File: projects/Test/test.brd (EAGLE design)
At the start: 63.5 x 24.1 mm, 47 parts, among them J2 1755529, U1 STM32F405RGT6, U2 CSD88584Q5DCT, U3 CSD88584Q5DCT, U4 CSD88584Q5DCT, Y1 ECS-80-S-4X

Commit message: some stuff
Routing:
- net 3V3: track 76.5 -> 71.3 mm, vias 8 -> 7
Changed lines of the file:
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@@
 <via x="34.29" y="16.764" extent="1-16" drill="0.35"/>
 <via x="46.482" y="16.256" extent="1-16" drill="0.35"/>
-<via x="46.482" y="5.461" extent="1-16" drill="0.35"/>
+<via x="46.482" y="5.969" extent="1-16" drill="0.35"/>
 <via x="34.417" y="6.223" extent="1-16" drill="0.35"/>
 </signal>
@@
 <wire x1="44.136" y1="15.053" x2="43.815" y2="14.732" width="0.2032" layer="1"/>
 <via x="43.815" y="14.732" extent="1-16" drill="0.35"/>
-<via x="37.6682" y="15.2301" extent="1-16" drill="0.35"/>
-<wire x1="38.136" y1="16.5481" x2="38.136" y2="15.6979" width="0.2032" layer="1"/>
-<wire x1="38.136" y1="15.6979" x2="37.6682" y2="15.2301" width="0.2032" layer="1"/>
-<wire x1="43.815" y1="14.732" x2="43.307" y2="14.224" width="0.2032" layer="16"/>
-<wire x1="43.307" y1="14.224" x2="42.4044" y2="14.224" width="0.2032" layer="16"/>
+<wire x1="38.136" y1="15.6979" x2="38.136" y2="16.5481" width="0.2032" layer="1"/>
 <wire x1="37.25" y1="14.224" x2="37.25" y2="14.6341" width="0.2032" layer="16"/>
-<wire x1="37.25" y1="14.6341" x2="37.8714" y2="15.2555" width="0.2032" layer="16"/>
-<via x="37.8714" y="15.2555" extent="1-16" drill="0.35"/>
-<wire x1="38.136" y1="16.5481" x2="38.136" y2="15.5201" width="0.2032" layer="1"/>
-<wire x1="38.136" y1="15.5201" x2="37.8714" y2="15.2555" width="0.2032" layer="1"/>
-<wire x1="37.25" y1="14.224" x2="36.576" y2="14.224" width="0.2032" layer="16"/>
-<wire x1="36.576" y1="14.224" x2="36.068" y2="13.716" width="0.2032" layer="16"/>
 <via x="36.068" y="13.716" extent="1-16" drill="0.35"/>
 <wire x1="34.7599" y1="13.672" x2="36.024" y2="13.672" width="0.2032" layer="1"/>
@@
 <wire x1="40.64" y1="12.4578" x2="42.3418" y2="12.4578" width="0.4064" layer="16"/>
 <wire x1="42.3418" y1="12.4578" x2="42.3858" y2="12.4138" width="0.4064" layer="16"/>
-<wire x1="37.6682" y1="15.2301" x2="37.25" y2="14.8119" width="0.2032" layer="16"/>
-<wire x1="37.25" y1="14.8119" x2="37.25" y2="14.224" width="0.2032" layer="16"/>
+<wire x1="37.25" y1="14.224" x2="37.25" y2="14.8119" width="0.2032" layer="16"/>
 <wire x1="36.068" y1="13.716" x2="36.576" y2="14.224" width="0.2032" layer="16"/>
 <wire x1="36.576" y1="14.224" x2="37.25" y2="14.224" width="0.2032" layer="16"/>
@@
 <wire x1="43.815" y1="14.732" x2="43.307" y2="14.224" width="0.2032" layer="16"/>
 <wire x1="43.307" y1="14.224" x2="42.4044" y2="14.224" width="0.2032" layer="16"/>
+<wire x1="37.25" y1="14.8119" x2="37.6781" y2="15.24" width="0.2032" layer="16"/>
+<wire x1="37.6781" y1="15.24" x2="37.719" y2="15.24" width="0.2032" layer="16"/>
+<via x="37.719" y="15.24" extent="1-16" drill="0.35"/>
+<wire x1="37.719" y1="15.24" x2="37.719" y2="15.2809" width="0.2032" layer="1"/>
+<wire x1="37.719" y1="15.2809" x2="38.136" y2="15.6979" width="0.2032" layer="1"/>
 </signal>
 <signal name="N$5">
@@
 <contactref element="U$2" pad="28"/>
 <wire x1="31.5468" y1="6.5532" x2="33.274" y2="4.826" width="0.2032" layer="1"/>
-<wire x1="33.274" y1="4.826" x2="36.1661" y2="4.826" width="0.2032" layer="1"/>
-<wire x1="36.1661" y1="4.826" x2="36.636" y2="5.2959" width="0.2032" layer="1"/>
+<wire x1="33.274" y1="4.826" x2="36.5471" y2="4.826" width="0.2032" layer="1"/>
+<wire x1="36.636" y1="4.9149" x2="36.636" y2="5.2959" width="0.2032" layer="1"/>
+<wire x1="36.636" y1="4.9149" x2="36.5471" y2="4.826" width="0.2032" layer="1"/>
 <wire x1="28.662" y1="8.148" x2="28.7149" y2="8.0951" width="0.2032" layer="1"/>
 <wire x1="28.7149" y1="8.0951" x2="29.18825" y2="8.0951" width="0.2032" layer="1"/>
@@
 <mfgpreviewcolor name="substratecolor" color="0xFF786E46"/>
 </mfgpreviewcolors>
-<errors>
-</errors>
 </board>
 </drawing>

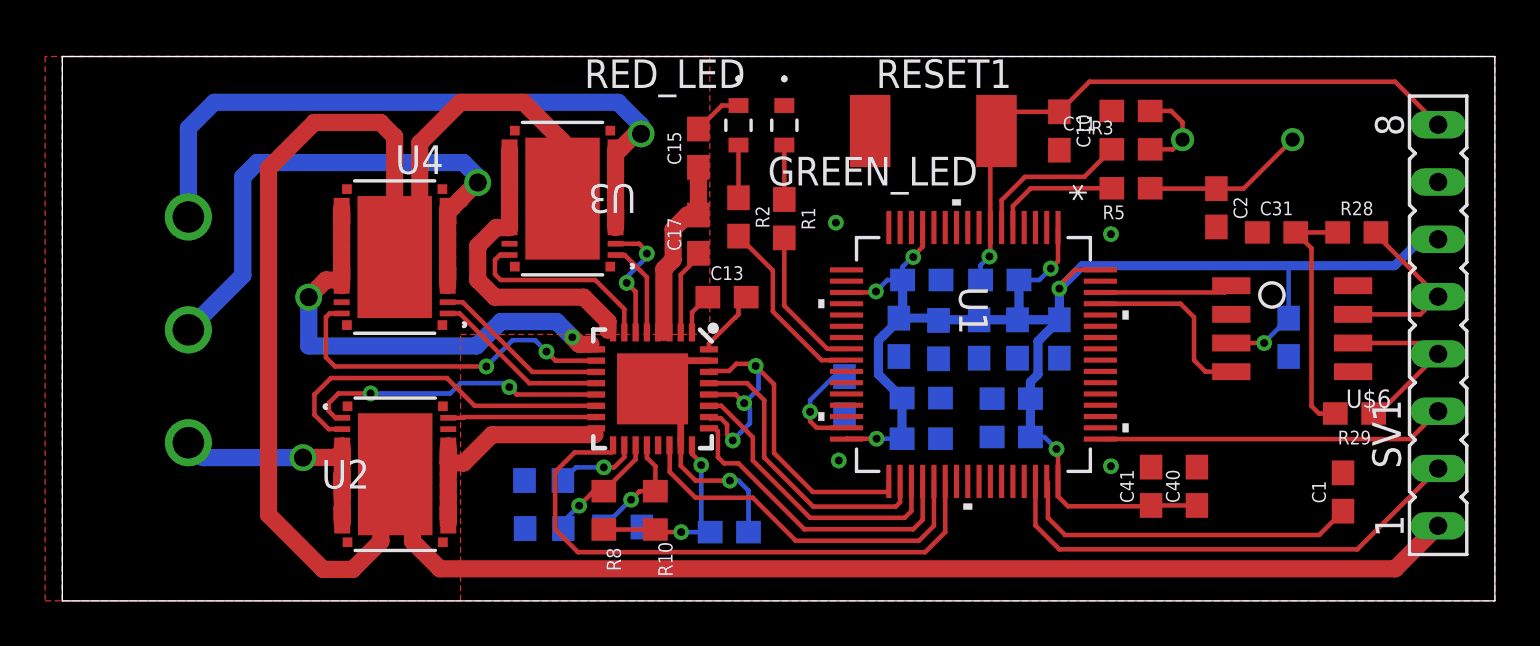
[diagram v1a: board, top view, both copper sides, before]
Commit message: Finished test board (before ratsnest)
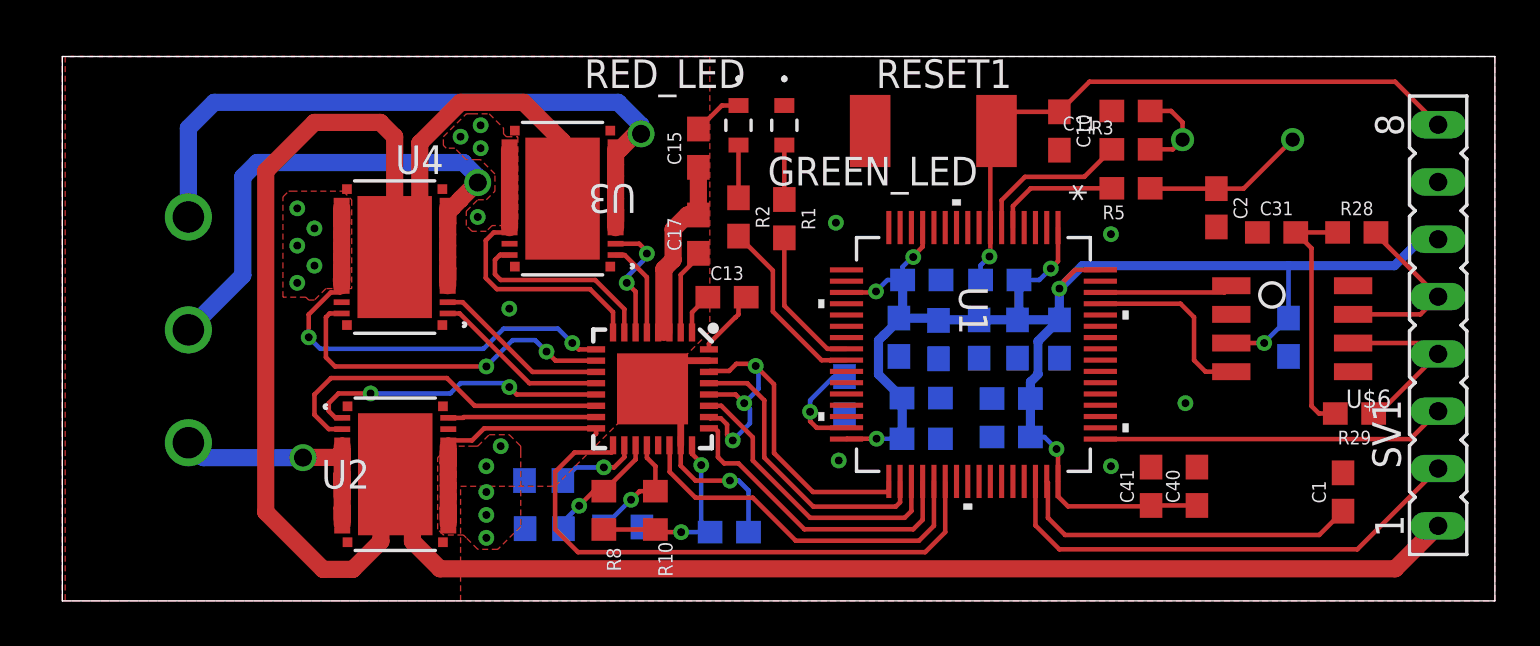
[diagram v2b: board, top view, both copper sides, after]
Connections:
- removed net SLA_1: U$2.8, U3.12, U3.13, U3.14, U3.15, U3.16, U3.17, U3.18, U3.19, U3.20
- removed net SLB_1: U$2.9, U4.12, U4.13, U4.14, U4.15, U4.16, U4.17, U4.18, U4.19, U4.20
- removed net SLC_1: U$2.16, U2.12, U2.13, U2.14, U2.15, U2.16, U2.17, U2.18, U2.19, U2.20
- net GND: now also U$2.16, U$2.8, U$2.9, U2.12, U2.13, U2.14, U2.15, U2.16, U2.17, U2.18, U2.19, U2.20, U3.12, U3.13, U3.14, U3.15, U3.16, U3.17, U3.18, U3.19, U3.20, U4.12, U4.13, U4.14, U4.15, U4.16, U4.17, U4.18, U4.19, U4.20
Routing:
- net GND: track 18.3 -> 67.7 mm, vias 5 -> 23
- net SLB_1: track 23.1 -> 0.00 mm, vias 2 -> 0
- net SLA_1: track 15.2 -> 0.00 mm
- net SLC_1: track 12.8 -> 0.00 mm

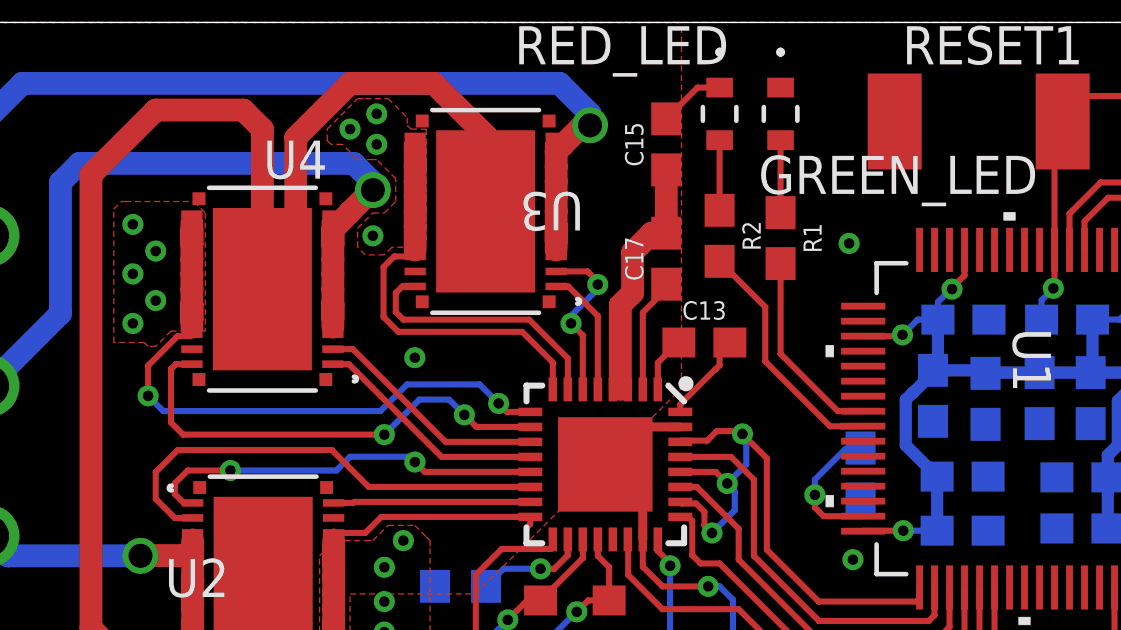
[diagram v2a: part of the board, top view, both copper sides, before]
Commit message: finished test board (after ratsnest and a few tweaks)
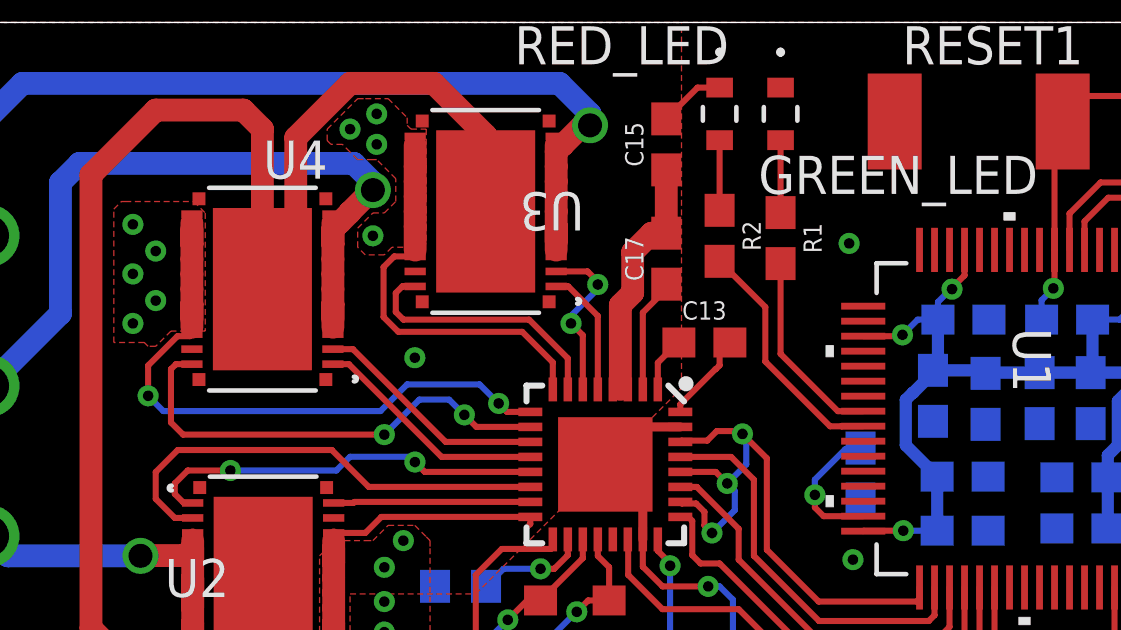
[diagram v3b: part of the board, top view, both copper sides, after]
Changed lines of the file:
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@@
 <wire x1="12.382" y1="16.24" x2="12.382" y2="16.74" width="0.762" layer="1"/>
 <wire x1="12.382" y1="16.74" x2="12.382" y2="17.24" width="0.762" layer="1"/>
-<wire x1="12.382" y1="14.24" x2="12.366" y2="14.224" width="0.762" layer="1"/>
 <wire x1="12.382" y1="14.24" x2="12.382" y2="13.97" width="0.2032" layer="1"/>
 <wire x1="12.382" y1="13.97" x2="12.382" y2="13.74" width="0.2032" layer="1"/>
@@
 <vertex x="20.32" y="3.302"/>
 </polygon>
-<wire x1="52.9726" y1="16.3322" x2="60.9854" y2="18.5674" width="0" layer="19" extent="1-1"/>
-<wire x1="51.1556" y1="16.5744" x2="52.9726" y2="16.3322" width="0" layer="19" extent="1-1"/>
-<wire x1="51.816" y1="12.7" x2="52.9726" y2="16.3322" width="0" layer="19" extent="1-1"/>
-<wire x1="54.356" y1="10.834" x2="51.816" y2="12.7" width="0" layer="19" extent="1-16"/>
-<wire x1="49.784" y1="8.763" x2="51.816" y2="12.7" width="0" layer="19" extent="1-1"/>
-<wire x1="50.292" y1="5.93" x2="49.784" y2="8.763" width="0" layer="19" extent="1-1"/>
-<wire x1="48.26" y1="5.93" x2="50.292" y2="5.93" width="0" layer="19" extent="1-1"/>
-<wire x1="46.482" y1="5.969" x2="48.26" y2="5.93" width="0" layer="19" extent="1-1"/>
-<wire x1="46.482" y1="16.256" x2="51.1556" y2="16.5744" width="0" layer="19" extent="1-1"/>
-<wire x1="46.0121" y1="14.172" x2="46.482" y2="16.256" width="0" layer="19" extent="1-1"/>
-<wire x1="46.0121" y1="12.672" x2="46.0121" y2="14.172" width="0" layer="19" extent="1-1"/>
-<wire x1="44.196" y1="10.7578" x2="46.0121" y2="12.672" width="0" layer="19" extent="1-16"/>
-<wire x1="42.3418" y1="10.7578" x2="44.196" y2="10.7578" width="0" layer="19" extent="16-16"/>
-<wire x1="40.64" y1="10.7578" x2="42.3418" y2="10.7578" width="0" layer="19" extent="16-16"/>
-<wire x1="38.8366" y1="10.7324" x2="40.64" y2="10.7578" width="0" layer="19" extent="16-16"/>
-<wire x1="37.084" y1="10.834" x2="38.8366" y2="10.7324" width="0" layer="19" extent="16-16"/>
-<wire x1="38.9246" y1="8.9916" x2="38.8366" y2="10.7324" width="0" layer="19" extent="16-16"/>
-<wire x1="38.9246" y1="7.1882" x2="38.9246" y2="8.9916" width="0" layer="19" extent="16-16"/>
-<wire x1="41.2124" y1="8.9662" x2="40.64" y2="10.7578" width="0" layer="19" extent="16-16"/>
-<wire x1="41.2124" y1="7.2644" x2="41.2124" y2="8.9662" width="0" layer="19" extent="16-16"/>
-<wire x1="38.95" y1="14.224" x2="38.8366" y2="10.7324" width="0" layer="19" extent="16-16"/>
-<wire x1="38.636" y1="16.5481" x2="38.95" y2="14.224" width="0" layer="19" extent="1-16"/>
-<wire x1="34.671" y1="8.2432" x2="37.084" y2="10.834" width="0" layer="19" extent="16-16"/>
-<wire x1="34.417" y1="6.223" x2="34.671" y2="8.2432" width="0" layer="19" extent="16-16"/>
-<wire x1="34.7599" y1="14.172" x2="37.084" y2="10.834" width="0" layer="19" extent="1-16"/>
-<wire x1="34.29" y1="16.764" x2="34.7599" y2="14.172" width="0" layer="19" extent="1-1"/>
-<wire x1="35.808" y1="20.828" x2="34.29" y2="16.764" width="0" layer="19" extent="1-1"/>
-<wire x1="32.004" y1="21.9583" x2="35.808" y2="20.828" width="0" layer="19" extent="1-1"/>
-<wire x1="29.972" y1="21.9583" x2="32.004" y2="21.9583" width="0" layer="19" extent="1-1"/>
-<wire x1="44.196" y1="19.978" x2="46.482" y2="16.256" width="0" layer="19" extent="1-1"/>
-<wire x1="46.521" y1="21.717" x2="44.196" y2="19.978" width="0" layer="19" extent="1-1"/>
-<wire x1="29.591" y1="5.3312" x2="34.417" y2="6.223" width="0" layer="19" extent="1-1"/>
-<wire x1="24.412" y1="11.898" x2="26.162" y2="9.398" width="0" layer="19" extent="1-1"/>
-<wire x1="23.662" y1="11.148" x2="24.412" y2="11.898" width="0" layer="19" extent="1-1"/>
-<wire x1="11.176" y1="16.51" x2="12.382" y2="16.74" width="0" layer="19" extent="1-1"/>
-<wire x1="10.414" y1="15.748" x2="11.176" y2="16.51" width="0" layer="19" extent="1-1"/>
-<wire x1="10.414" y1="17.399" x2="11.176" y2="16.51" width="0" layer="19" extent="1-1"/>
-<wire x1="11.176" y1="14.859" x2="10.414" y2="15.748" width="0" layer="19" extent="1-1"/>
-<wire x1="10.414" y1="14.097" x2="11.176" y2="14.859" width="0" layer="19" extent="1-1"/>
-<wire x1="18.542" y1="20.066" x2="19.8242" y2="19.8308" width="0" layer="19" extent="1-1"/>
-<wire x1="18.542" y1="21.082" x2="18.542" y2="20.066" width="0" layer="19" extent="1-1"/>
-<wire x1="17.653" y1="20.574" x2="18.542" y2="20.066" width="0" layer="19" extent="1-1"/>
-<wire x1="18.415" y1="17.018" x2="19.8242" y2="16.8308" width="0" layer="19" extent="1-1"/>
-<wire x1="23.662" y1="7.648" x2="26.162" y2="9.398" width="0" layer="19" extent="1-1"/>
-<wire x1="18.796" y1="5.969" x2="17.1074" y2="6.1134" width="0" layer="19" extent="1-1"/>
-<wire x1="19.431" y1="6.858" x2="18.796" y2="5.969" width="0" layer="19" extent="1-1"/>
-<wire x1="18.796" y1="4.826" x2="18.796" y2="5.969" width="0" layer="19" extent="1-1"/>
-<wire x1="18.796" y1="3.81" x2="18.796" y2="4.826" width="0" layer="19" extent="1-1"/>
-<wire x1="18.796" y1="2.794" x2="18.796" y2="3.81" width="0" layer="19" extent="1-1"/>
-<wire x1="20.486" y1="5.334" x2="18.796" y2="4.826" width="0" layer="19" extent="16-16"/>
-<wire x1="20.5114" y1="3.2004" x2="18.796" y2="2.794" width="0" layer="19" extent="16-16"/>
-<wire x1="19.812" y1="12.954" x2="22.606" y2="11.43" width="0" layer="19" extent="1-1"/>
-<wire x1="25.6912" y1="3.2766" x2="27.412" y2="6.898" width="0" layer="19" extent="1-16"/>
-<wire x1="56.769" y1="5.676" x2="54.356" y2="10.834" width="0" layer="19" extent="1-16"/>
 </signal>
 <signal name="NRST">
@@
 <wire x1="15.8437" y1="16.3517" x2="14.732" y2="15.24" width="0.762" layer="1"/>
 <wire x1="15.8437" y1="20.2887" x2="15.8437" y2="16.3517" width="0.762" layer="1"/>
-<wire x1="22.1742" y1="17.8308" x2="28.194" y2="17.106" width="0" layer="19" extent="1-1"/>
 </signal>
 <signal name="CAN_H">
@@
 <via x="43.815" y="14.732" extent="1-16" drill="0.35"/>
 <wire x1="38.136" y1="15.6979" x2="38.136" y2="16.5481" width="0.2032" layer="1"/>
-<wire x1="37.25" y1="14.224" x2="37.25" y2="14.6341" width="0.2032" layer="16"/>
 <via x="36.068" y="13.716" extent="1-16" drill="0.35"/>
 <wire x1="34.7599" y1="13.672" x2="36.024" y2="13.672" width="0.2032" layer="1"/>
@@
 <wire x1="40.64" y1="12.4578" x2="42.3418" y2="12.4578" width="0.4064" layer="16"/>
 <wire x1="42.3418" y1="12.4578" x2="42.3858" y2="12.4138" width="0.4064" layer="16"/>
-<wire x1="37.25" y1="14.224" x2="37.25" y2="14.8119" width="0.2032" layer="16"/>
+<wire x1="37.25" y1="14.8119" x2="37.25" y2="14.224" width="0.2032" layer="16"/>
 <wire x1="36.068" y1="13.716" x2="36.576" y2="14.224" width="0.2032" layer="16"/>
 <wire x1="36.576" y1="14.224" x2="37.25" y2="14.224" width="0.2032" layer="16"/>
